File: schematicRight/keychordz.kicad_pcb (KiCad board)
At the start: 2 copper layers, 124 x 101 mm, 45 parts, among them IC1 MCP73833-BZI_UN, J1 USB_C_Receptacle_USB2.0, J2 Conn_01x04_Male, J3 Conn_01x04_Male, SW1 SW_Push, SW2 SW_Push, SW3 SW_Push, SW4 SW_Push, SW5 SW_Push, SW6 SW_Push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

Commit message: change right PCB to STM32
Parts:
- added AE1: PCB, RF_Antenna:Texas_SWRA117D_2.4GHz_Left, F.Cu at (18.8, 55.2)
- added C1: 1µF, Capacitor_SMD:C_0402_1005Metric_Pad0.74x0.62mm_HandSolder, F.Cu at (25.5, 30.8)
- added C10: 12pF, Capacitor_SMD:C_0603_1608Metric_Pad1.08x0.95mm_HandSolder, F.Cu at (36.2, 49.8)
- added C11: 12pF, Capacitor_SMD:C_0603_1608Metric_Pad1.08x0.95mm_HandSolder, F.Cu at (38.6, 47.4)
- added C12: 0.8pF, Capacitor_SMD:C_0201_0603Metric_Pad0.64x0.40mm_HandSolder, F.Cu at (23.7, 55.1)
- added C13: 1µF, Capacitor_SMD:C_0402_1005Metric_Pad0.74x0.62mm_HandSolder, F.Cu at (25.4, 38.9)
- added C14: 0.1µF, Capacitor_SMD:C_0402_1005Metric_Pad0.74x0.62mm_HandSolder, F.Cu at (44.7, 35.6)
- added C15: 12pF, Capacitor_SMD:C_0603_1608Metric_Pad1.08x0.95mm_HandSolder, F.Cu at (16.9, 39.8)
- added C18: 12pF, Capacitor_SMD:C_0603_1608Metric_Pad1.08x0.95mm_HandSolder, F.Cu at (16.8, 43.5)
- added C2: 1µF, Capacitor_SMD:C_0402_1005Metric_Pad0.74x0.62mm_HandSolder, F.Cu at (32.0, 30.2)
- added C3: 1µF, Capacitor_SMD:C_0402_1005Metric_Pad0.74x0.62mm_HandSolder, F.Cu at (39.2, 27.8)
- added C5: 1µF, Capacitor_SMD:C_0402_1005Metric_Pad0.74x0.62mm_HandSolder, F.Cu at (39.1, 30.3)
- added C6: 10µF, Capacitor_SMD:C_0402_1005Metric_Pad0.74x0.62mm_HandSolder, F.Cu at (32.0, 31.4)
- added C7: 1µF, Capacitor_SMD:C_0402_1005Metric_Pad0.74x0.62mm_HandSolder, F.Cu at (38.6, 42.6)
- added C8: 0.1µF, Capacitor_SMD:C_0402_1005Metric_Pad0.74x0.62mm_HandSolder, F.Cu at (24.9, 45.3)
- added C9: 100pF, Capacitor_SMD:C_0402_1005Metric_Pad0.74x0.62mm_HandSolder, F.Cu at (34.3, 51.7)
- added IC2: TPS7A2024PDBVR, SamacSys_Parts:SOT95P280X145-5N, F.Cu at (28.5, 31.4)
- added IC3: STM32WB55RGV7, SamacSys_Parts:QFN40P800X800X100-69N-D, F.Cu at (31.7, 43.3)
- added L1: 3.9nH, Inductor_SMD:L_0402_1005Metric_Pad0.77x0.64mm_HandSolder, F.Cu at (21.3, 55.1)
- added Q1: Q_PMOS_GSD, Package_TO_SOT_SMD:SC-59_Handsoldering, F.Cu at (44.5, 38.6)
- added R10: 10k, Resistor_SMD:R_0603_1608Metric_Pad0.98x0.95mm_HandSolder, F.Cu at (49.3, 38.6)
- added R8: 1k, Resistor_SMD:R_0603_1608Metric_Pad0.98x0.95mm_HandSolder, F.Cu at (40.6, 40.0)
- added R9: 1k, Resistor_SMD:R_0603_1608Metric_Pad0.98x0.95mm_HandSolder, F.Cu at (40.6, 36.6)
- added Y1: Crystal_GND23, Crystal:Crystal_SMD_2016-4Pin_2.0x1.6mm_HandSoldering, F.Cu at (38.5, 49.8)
- added Y2: Crystal, Crystal:Crystal_SMD_MicroCrystal_CC7V-T1A-2Pin_3.2x1.5mm_HandSoldering, F.Cu at (20.2, 41.4)
- J2: value Conn_01x04_Male -> DEBUG_CONN
- J3: value Conn_01x04_Male -> OLED_CONN
- U1: value nRF52840_Breakout -> MIC5504-3.3YM5; footprint schematic:nRF52840_Breakout -> Package_TO_SOT_SMD:SOT-23-5
- moved J2 16.7 mm to (28.1, 35.3), turned to 90 degrees
- moved U1 12.5 mm to (42.7, 29.8)
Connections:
- D4 pad 2: Net-(D4-Pad2) -> LED_IN
- J2 pad 1: SWDCLK -> SWO
- J2 pad 2: SWDIO -> SWCLK
- J2 pad 3: RST -> SWDIO
- J3 pad 2: Net-(J3-Pad2) -> 2.4V
- J3 pad 3: Net-(U1-PadK2) -> SCK
- J3 pad 4: Net-(J3-Pad4) -> MOSI
- J3 pad 5: Net-(U1-PadM2) -> OLED_RES
- J3 pad 6: Net-(U1-PadN1) -> OLED_DC
- J3 pad 7: Net-(U1-PadP2) -> OLED_CS
- SW1 pad 1: Net-(SW1-Pad1) -> BTN1
- SW2 pad 1: Net-(SW2-Pad1) -> BTN2
- SW3 pad 1: Net-(SW3-Pad1) -> BTN3
- SW4 pad 1: Net-(SW4-Pad1) -> BTN4
- SW5 pad 1: Net-(SW5-Pad1) -> BTN5
- SW6 pad 1: Net-(SW6-Pad1) -> BTN6
- SW7 pad 1: Net-(SW7-Pad1) -> BTN7
- SW9 pad 1: V_BAT -> V_BAT_SW
- SW9 pad 4: (no net) -> V_BAT
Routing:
- net GND: track 577.2 -> 143.7 mm, vias 15 -> 43
- net BTN6: track 0.00 -> 142.5 mm, vias 0 -> 2
- net 2.4V: track 0.00 -> 129.6 mm, vias 0 -> 7
- net BTN7: track 0.00 -> 114.2 mm, vias 0 -> 2
- net Net-(SW6-Pad1): track 95.7 -> 0.00 mm, vias 1 -> 0
- net MOSI: track 0.00 -> 85.8 mm, vias 0 -> 4
- net BTN5: track 0.00 -> 81.3 mm, vias 0 -> 2
- net SCK: track 0.00 -> 76.2 mm, vias 0 -> 2
- net Net-(J3-Pad2): track 73.6 -> 0.00 mm
- net BTN1: track 0.00 -> 71.3 mm, vias 0 -> 1
- net OLED_RES: track 0.00 -> 71.2 mm, vias 0 -> 2
- net Net-(SW7-Pad1): track 71.1 -> 0.00 mm, vias 1 -> 0
- net Net-(D4-Pad2): track 69.0 -> 0.00 mm
- net OLED_DC: track 0.00 -> 67.8 mm, vias 0 -> 2
- net BTN4: track 0.00 -> 65.8 mm, vias 0 -> 2
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- added copper zone on B.Cu, net GND
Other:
- board text added: "CL"
- board text added: "IO"
- board text added: "SWO"
- board text removed: "RST"
- board text removed: "SWDCLK"
- board text removed: "SWDIO"

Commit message: change OLED voltage to V_BAT (ordered this commit)
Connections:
- J3 pad 2: 2.4V -> V_BAT
- SW9 pad 1: V_BAT_SW -> V_BAT
- SW9 pad 4: V_BAT -> (no net)
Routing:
- net 2.4V: track 129.6 -> 67.2 mm
- net V_BAT: track 291.9 -> 297.6 mm

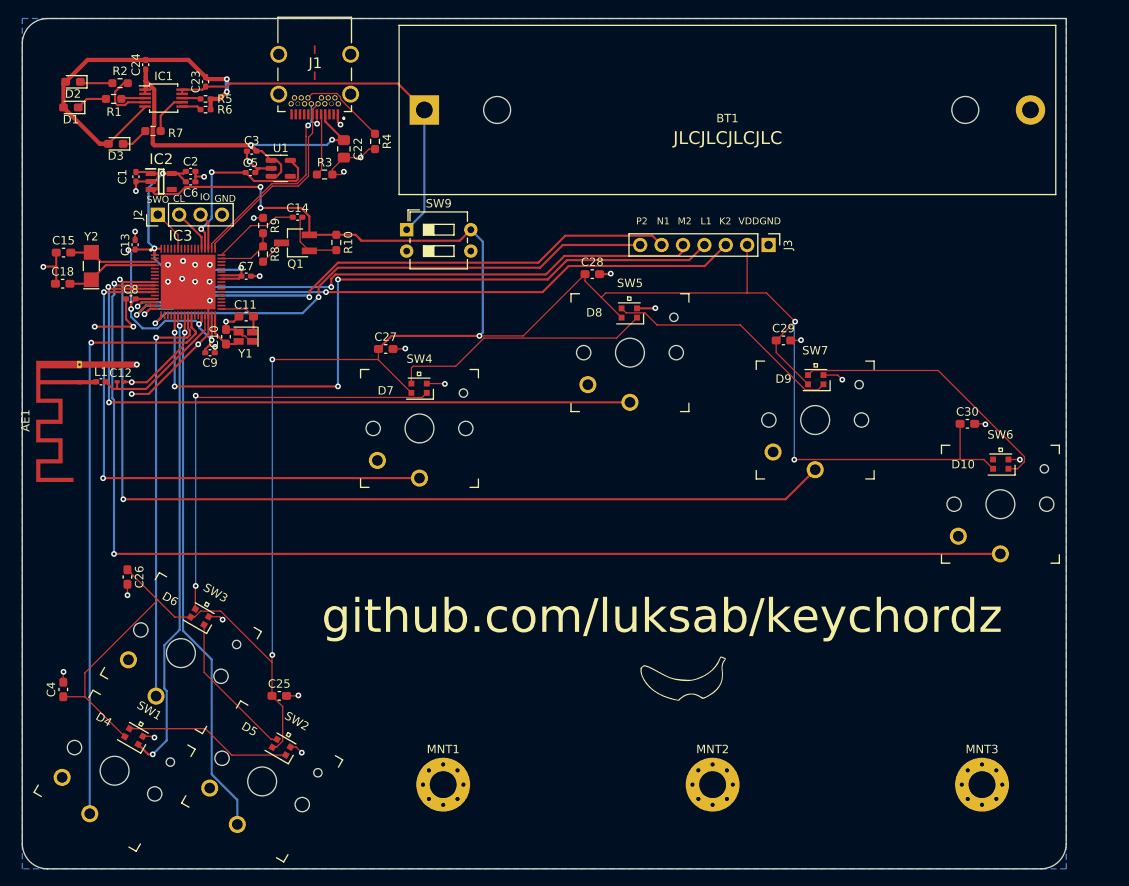
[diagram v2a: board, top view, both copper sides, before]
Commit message: use Arduino pro micro
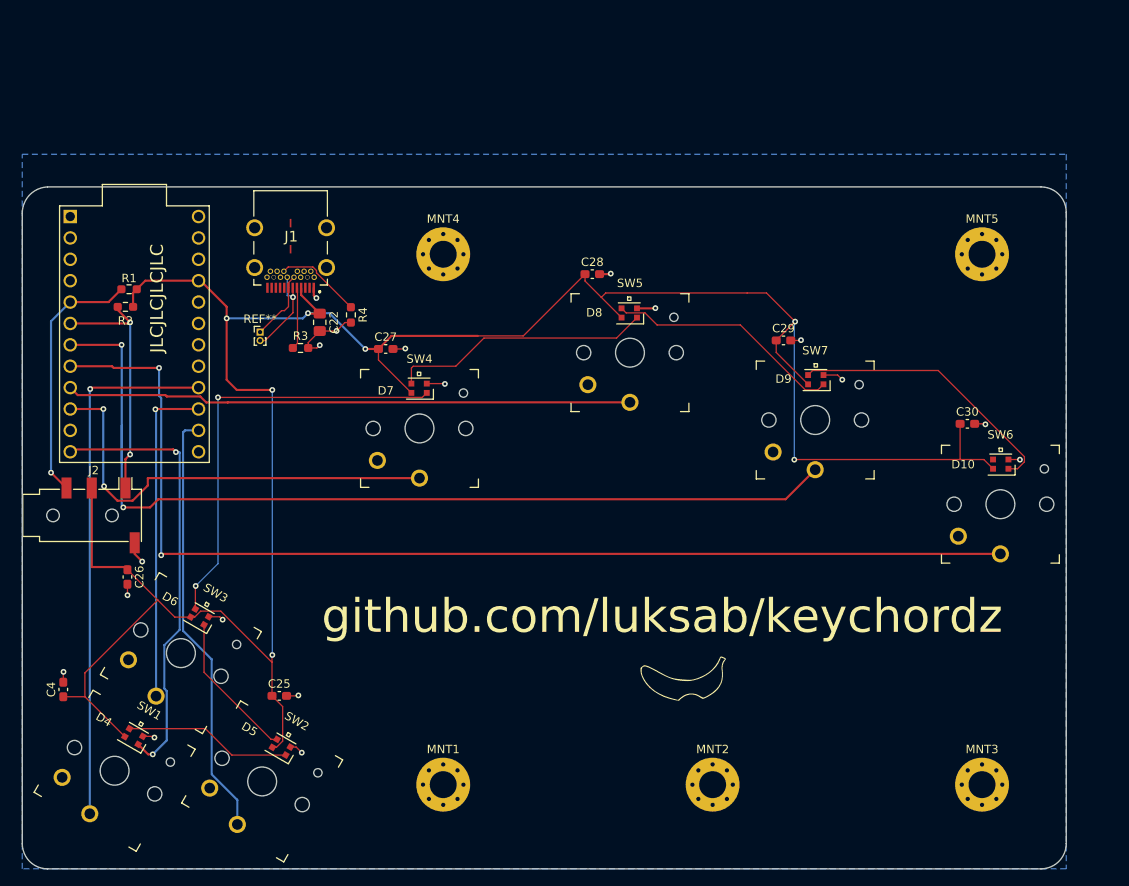
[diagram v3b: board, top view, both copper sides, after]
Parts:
- removed AE1: PCB, RF_Antenna:Texas_SWRA117D_2.4GHz_Left
- removed BT1: Battery_Cell, Battery:BatteryHolder_MPD_BH-18650-PC2
- removed C1, C13, C2, C23, C24, C3, C5, C7: 1µF, Capacitor_SMD:C_0402_1005Metric_Pad0.74x0.62mm_HandSolder
- removed C10, C11, C15, C18: 12pF, Capacitor_SMD:C_0603_1608Metric_Pad1.08x0.95mm_HandSolder
- removed C12: 0.8pF, Capacitor_SMD:C_0201_0603Metric_Pad0.64x0.40mm_HandSolder
- removed C14, C8: 0.1µF, Capacitor_SMD:C_0402_1005Metric_Pad0.74x0.62mm_HandSolder
- removed C6: 10µF, Capacitor_SMD:C_0402_1005Metric_Pad0.74x0.62mm_HandSolder
- removed C9: 100pF, Capacitor_SMD:C_0402_1005Metric_Pad0.74x0.62mm_HandSolder
- removed D1, D2, D3: LED_Small, LED_SMD:LED_0603_1608Metric_Pad1.05x0.95mm_HandSolder
- removed IC1: MCP73833-BZI_UN, Package_SO:MSOP-10_3x3mm_P0.5mm
- removed IC2: TPS7A2024PDBVR, SamacSys_Parts:SOT95P280X145-5N
- removed IC3: STM32WB55RGV7, SamacSys_Parts:QFN40P800X800X100-69N-D
- removed J3: OLED_CONN, Connector_PinHeader_2.54mm:PinHeader_1x07_P2.54mm_Vertical
- removed L1: 3.9nH, Inductor_SMD:L_0402_1005Metric_Pad0.77x0.64mm_HandSolder
- removed Q1: Q_PMOS_GSD, Package_TO_SOT_SMD:SC-59_Handsoldering
- removed R10: 10k, Resistor_SMD:R_0603_1608Metric_Pad0.98x0.95mm_HandSolder
- removed R5: 10k, Resistor_SMD:R_0402_1005Metric_Pad0.72x0.64mm_HandSolder
- removed R6: 1k, Resistor_SMD:R_0402_1005Metric_Pad0.72x0.64mm_HandSolder
- removed R7: 470, Resistor_SMD:R_0603_1608Metric_Pad0.98x0.95mm_HandSolder
- removed R8, R9: 1k, Resistor_SMD:R_0603_1608Metric_Pad0.98x0.95mm_HandSolder
- removed SW9: SW_SPST, Button_Switch_THT:SW_DIP_SPSTx02_Slide_6.7x6.64mm_W7.62mm_P2.54mm_LowProfile
- removed Y1: Crystal_GND23, Crystal:Crystal_SMD_2016-4Pin_2.0x1.6mm_HandSoldering
- removed Y2: Crystal, Crystal:Crystal_SMD_MicroCrystal_CC7V-T1A-2Pin_3.2x1.5mm_HandSoldering
- added MNT4: MountingHole_3.2mm_M3_Pad_Via, MountingHole:MountingHole_3.2mm_M3_Pad_Via, F.Cu at (62.0, 40.0)
- added MNT5: MountingHole_3.2mm_M3_Pad_Via, MountingHole:MountingHole_3.2mm_M3_Pad_Via, F.Cu at (126.0, 40.0)
- added REF**: PinHeader_1x02_P1.00mm_Vertical, Connector_PinHeader_1.00mm:PinHeader_1x02_P1.00mm_Vertical, F.Cu at (40.2, 49.2)
- J2: value DEBUG_CONN -> AudioPlug4; footprint Connector_PinHeader_2.54mm:PinHeader_1x04_P2.54mm_Vertical -> Connector_Audio:Jack_3.5mm_PJ320D_Horizontal
- R1, R2: value 470 -> R_Small
- U1: value MIC5504-3.3YM5 -> ProMicro; footprint Package_TO_SOT_SMD:SOT-23-5 -> promicro:ProMicro
- moved J2 36.5 mm to (20.4, 71.0), turned to 0 degrees
- moved R2 26.6 mm to (24.2, 46.2)
- moved U1 26.3 mm to (25.3, 49.5), turned to -90 degrees
- moved R1 22.7 mm to (24.7, 44.2), turned to 180 degrees
- moved C22 20.8 mm to (47.3, 48.1)
- moved J1 20.8 mm to (43.9, 38.5)
- moved R3 20.8 mm to (45.0, 51.1)
- moved R4 20.8 mm to (51.0, 47.2)
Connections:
- C25 pad 1: V_BAT -> +5V
- C26 pad 1: V_BAT -> +5V
- C27 pad 1: V_BAT -> +5V
- C28 pad 1: V_BAT -> +5V
- C29 pad 1: V_BAT -> +5V
- C30 pad 1: V_BAT -> +5V
- C4 pad 1: V_BAT -> +5V
- D10 pad 1: V_BAT -> +5V
- D4 pad 1: V_BAT -> +5V
- D5 pad 1: V_BAT -> +5V
- D6 pad 1: V_BAT -> +5V
- D7 pad 1: V_BAT -> +5V
- D8 pad 1: V_BAT -> +5V
- D9 pad 1: V_BAT -> +5V
- R1 pad 1: Net-(D1-Pad1) -> +5V
- R1 pad 2: Net-(IC1-Pad3) -> SDA
- R2 pad 1: Net-(D2-Pad1) -> SCK
- R2 pad 2: Net-(IC1-Pad4) -> +5V
- U1 pad 1: +5V -> unconnected-(U1-Pad1)
- U1 pad 2: GND -> unconnected-(U1-Pad2)
- U1 pad 3: +5V -> GND
- U1 pad 4: unconnected-(U1-Pad4) -> GND
- U1 pad 5: 3.3V_USB -> SDA
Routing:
- net V_BAT: track 297.6 -> 0.00 mm, vias 7 -> 0
- net +5V: track 44.7 -> 280.8 mm, vias 2 -> 7
- net GND: track 143.7 -> 34.6 mm, vias 43 -> 18
- net MOSI: track 85.8 -> 0.00 mm, vias 4 -> 0
- net OLED_RES: track 71.2 -> 0.00 mm, vias 2 -> 0
- net OLED_DC: track 67.8 -> 0.00 mm, vias 2 -> 0
- net 2.4V: track 67.2 -> 0.00 mm, vias 7 -> 0
- net OLED_CS: track 63.4 -> 0.00 mm, vias 2 -> 0
- net SCK: track 76.2 -> 29.5 mm
- net V_BAT_SW: track 46.0 -> 0.00 mm
- net SDA: track 0.00 -> 30.5 mm, vias 0 -> 1
- net 3.3V_USB: track 23.2 -> 0.00 mm, vias 2 -> 0
- net Net-(C12-Pad1): track 17.7 -> 0.00 mm
- net USB_D-: track 24.1 -> 8.38 mm
- net USB_D+: track 26.1 -> 11.2 mm, vias 2 -> 1
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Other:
- board size 124 x 101 mm -> 124 x 81 mm
- board text removed: "CL"
- board text removed: "GND"
- board text removed: "IO"
- board text removed: "K2"
- board text removed: "L1"
- board text removed: "M2"
- board text removed: "N1"
- board text removed: "P2"
- board text removed: "SWO"
- board text removed: "VDD"

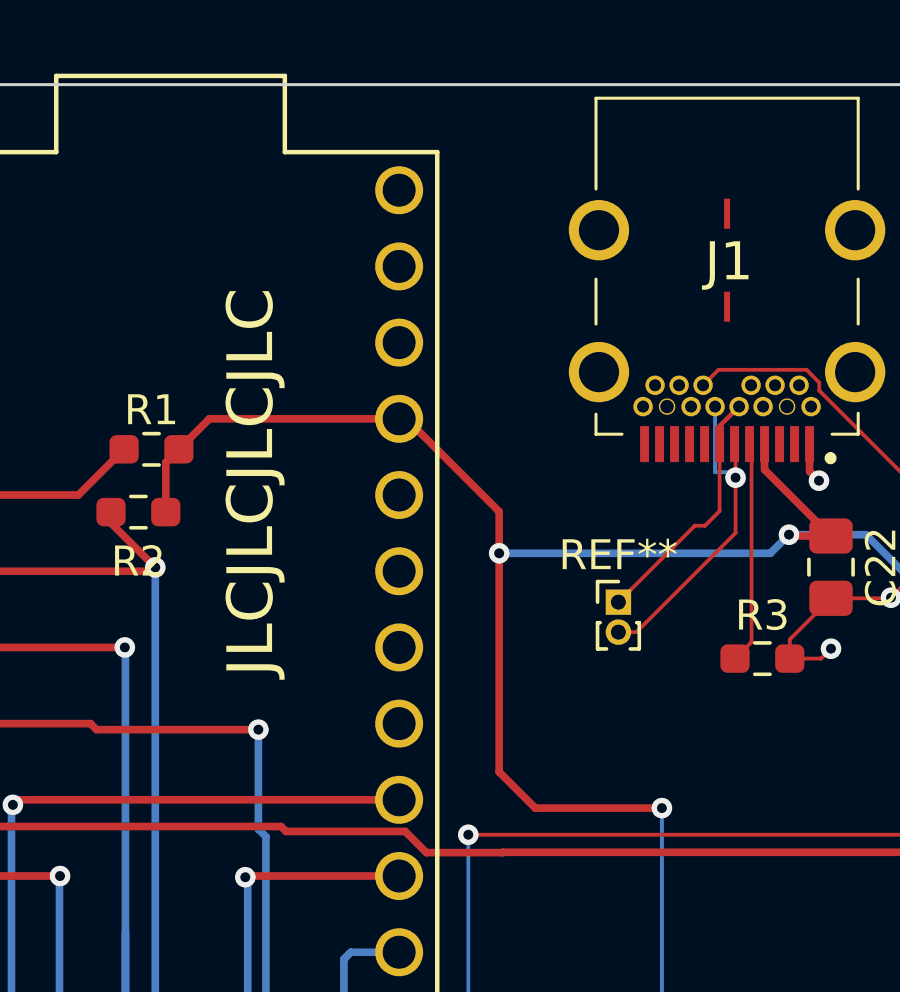
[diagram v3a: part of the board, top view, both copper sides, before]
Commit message: fix LED vcc
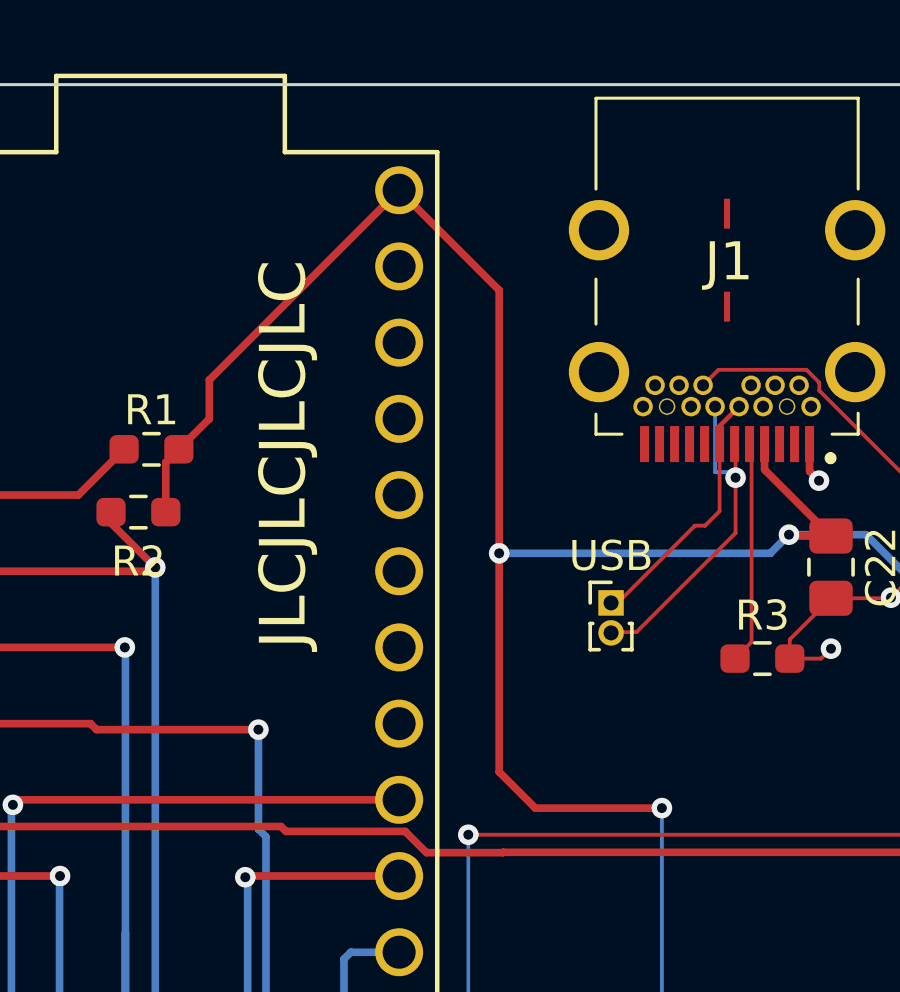
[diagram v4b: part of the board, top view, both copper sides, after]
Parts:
- removed REF**: PinHeader_1x02_P1.00mm_Vertical, Connector_PinHeader_1.00mm:PinHeader_1x02_P1.00mm_Vertical
- added USB: PinHeader_1x02_P1.00mm_Vertical, Connector_PinHeader_1.00mm:PinHeader_1x02_P1.00mm_Vertical, F.Cu at (40.0, 49.3)
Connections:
- U1 pad 21: +5V -> unconnected-(U1-Pad21)
- U1 pad 24: unconnected-(U1-Pad24) -> +5V
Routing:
- net +5V: track 280.8 -> 292.5 mm
